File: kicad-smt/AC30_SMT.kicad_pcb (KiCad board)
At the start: 2 copper layers, 173 x 82 mm, 119 parts, among them IC1 4013, IC10 555, IC11 4001, IC12 1489, IC13 4070, IC14 4053, IC15 1488, IC2 4001, IC3 4070, IC4 4558, IC5 4013, IC6 4053, IC7 4049, IC8 4013, IC9 4023, J1 Front panel harness 1, J12 Power input, J2 Front panel harness 2, J3 Computer interface (COMP), J4 Control interface, J5 Terminal interface (TERM), Q1 MMBT5088, Q10 MMBT5087, Q11 MMBT5087, Q2 MMBT5088, Q3 MMBT5087, Q4 MMBT5088, Q5 MMBT5088, Q6 MMBT5088, Q7 MMBT5088, Q8 MMBT5088, Q9 MMBT5087

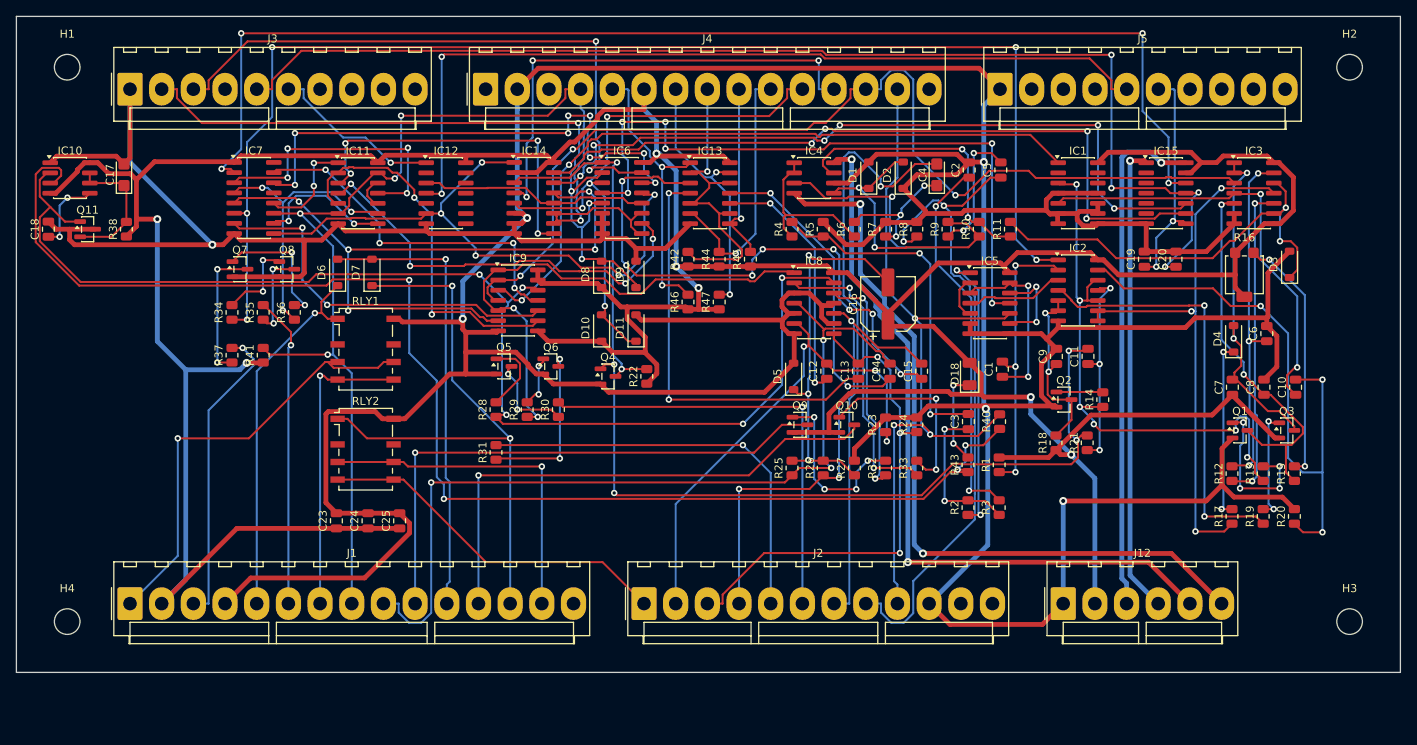
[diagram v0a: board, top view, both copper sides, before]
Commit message: SMT board: through-hole jumper pads for the front panel
Replace the J1/J2 KK-396 front-panel harness headers on the SMT board with
five rows of 0.1 in through-hole wire pads along the bottom edge, each pad
labelled with its net name on the silkscreen:
J1 SWITCHES, J2 LEDS, J13 MOTOR, J14 MIC (AUDIO_OUT), J15 EAR (AUDIO_IN).

The through-hole board keeps J1/J2. SMT board is now 173.0 x 89.0 mm;
ERC, DRC (all severities) and parity clean, fully routed.
AC30-SMT-settings.md updated.

Co-Authored-By: Claude Opus 5.5 <noreply@anthropic.com>
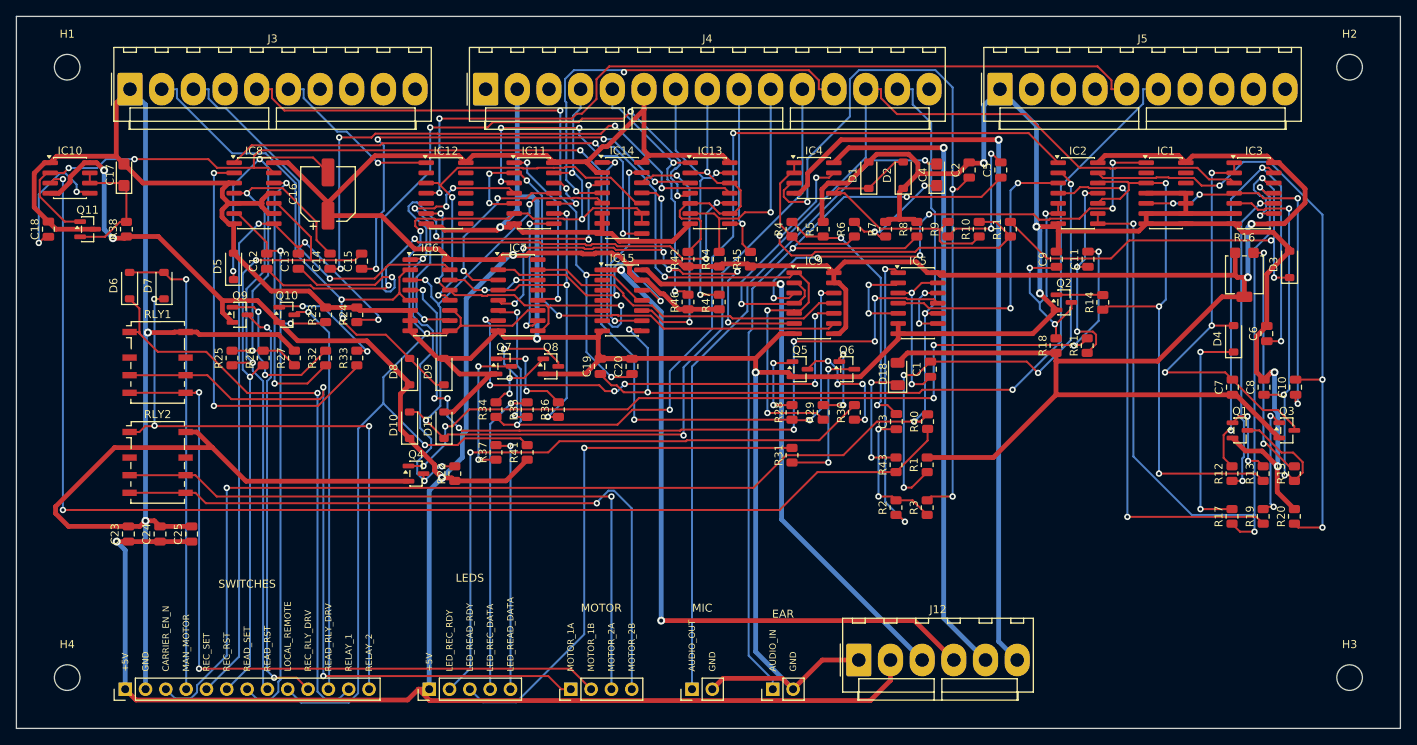
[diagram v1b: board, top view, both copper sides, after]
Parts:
- added J13: MOTOR, Connector_PinHeader_2.54mm:PinHeader_1x04_P2.54mm_Vertical, F.Cu at (99.3, 113.6)
- added J14: MIC, Connector_PinHeader_2.54mm:PinHeader_1x02_P2.54mm_Vertical, F.Cu at (114.5, 113.6)
- added J15: EAR, Connector_PinHeader_2.54mm:PinHeader_1x02_P2.54mm_Vertical, F.Cu at (124.5, 113.6)
- J1: value Front panel harness 1 -> SWITCHES; footprint Connector_Molex:Molex_KK-396_A-41791-0015_1x15_P3.96mm_Vertical -> Connector_PinHeader_2.54mm:PinHeader_1x13_P2.54mm_Vertical
- J2: value Front panel harness 2 -> LEDS; footprint Connector_Molex:Molex_KK-396_A-41791-0012_1x12_P3.96mm_Vertical -> Connector_PinHeader_2.54mm:PinHeader_1x05_P2.54mm_Vertical
- moved C12 71.3 mm to (61.3, 60.1)
- moved Q10 71.3 mm to (63.8, 66.8)
- moved R24 71.3 mm to (72.5, 66.8)
- moved R33 71.3 mm to (72.5, 72.2)
- moved C13 71.3 mm to (65.2, 60.1)
- moved C15 71.3 mm to (73.2, 60.1)
- moved D5 71.3 mm to (57.1, 60.8)
- moved Q9 71.3 mm to (58.0, 66.8)
- moved R23 71.3 mm to (68.7, 66.8)
- moved R25 71.3 mm to (57.0, 72.2)
- moved R26 71.3 mm to (60.9, 72.2)
- moved R27 71.3 mm to (64.8, 72.2)
- moved R32 71.3 mm to (68.7, 72.2)
- moved C14 71.3 mm to (69.2, 60.1)
- moved C16 71.3 mm to (69.0, 51.7)
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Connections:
- J1 pad 1: /MOTOR_1A -> +5V
- J1 pad 11: /MAN_MOTOR -> /READ_RLY_DRV
- J1 pad 12: /READ_RLY_DRV -> /RELAY_1
- J1 pad 2: +5V -> GND
- J1 pad 3: /LED_READ_DATA -> CARRIER_EN_N
- J1 pad 4: GND -> /MAN_MOTOR
- J1 pad 5: /RELAY_1 -> /REC_SET
- J1 pad 6: /LED_REC_DATA -> /REC_RST
- J1 pad 7: /MOTOR_1B -> /READ_SET
- J1 pad 8: /LOCAL_REMOTE -> /READ_RST
- J1 pad 9: /READ_RST -> /LOCAL_REMOTE
- J2 pad 1: /MOTOR_2B -> +5V
- J2 pad 2: /READ_SET -> /LED_REC_RDY
- J2 pad 3: /REC_SET -> /LED_READ_RDY
- J2 pad 4: /REC_RST -> /LED_REC_DATA
- J2 pad 5: /LED_READ_RDY -> /LED_READ_DATA
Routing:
- net /CPU_RX: track 154.6 -> 30.7 mm, vias 4 -> 2
- net +5V: track 542.4 -> 657.7 mm
- net /TERM_RS232_IN: track 28.3 -> 109.4 mm, vias 2 -> 3
- net CARRIER_EN_N: track 95.6 -> 170.5 mm
- net /TERM_ECHO: track 93.1 -> 24.7 mm, vias 4 -> 2
- net GND: track 778.5 -> 713.4 mm, vias 6 -> 10
- net /TERM_TX_SEL: track 93.6 -> 30.3 mm, vias 6 -> 2
- net /CPU_RS232_IN: track 149.9 -> 86.6 mm, vias 4 -> 3
- net /TERM_CLK_OUT: track 73.1 -> 133.1 mm
- net /MOTOR_1B: track 37.9 -> 93.3 mm, vias 1 -> 2
- net /DATA_SEL: track 66.7 -> 12.0 mm, vias 8 -> 2
- net /READ_EN: track 65.5 -> 114.8 mm, vias 2 -> 4
- net /MOTOR_2B: track 44.7 -> 87.5 mm, vias 0 -> 1
- net /MOTOR_2A: track 42.9 -> 85.4 mm
- net DATA_IN: track 162.2 -> 119.8 mm, vias 5 -> 4
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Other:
- board size 173 x 82 mm -> 173 x 89 mm
- board text added: "+5V"
- board text added: "AUDIO_IN"
- board text added: "AUDIO_OUT"
- board text added: "CARRIER_EN_N"
- board text added: "GND"
- board text added: "LED_READ_DATA"
- board text added: "LED_READ_RDY"
- board text added: "LED_REC_DATA"
- board text added: "LED_REC_RDY"
- board text added: "LOCAL_REMOTE"
- board text added: "MAN_MOTOR"
- board text added: "MOTOR_1A"
- board text added: "MOTOR_1B"
- board text added: "MOTOR_2A"
- board text added: "MOTOR_2B"
- board text added: "READ_RLY_DRV"
- board text added: "READ_RST"
- board text added: "READ_SET"
- board text added: "REC_RLY_DRV"
- board text added: "REC_RST"
- board text added: "REC_SET"
- board text added: "RELAY_1"
- board text added: "RELAY_2"

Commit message: SMT board: separate MIC A/B and EAR A/B jumper pads
Each front-panel jack now has its own tip and GND pads (J14 MIC: MIC_A,
GND, MIC_B, GND; J15 EAR: EAR_A, GND, EAR_B, GND). The S2/S3 audio poles
wire to new SWITCHES pads (AUDIO_OUT, MIC_A/B, AUDIO_IN, EAR_A/B) and the
board joins them. SMT board is now 173.0 x 88.5 mm; ERC, DRC (all
severities) and parity clean, fully routed. AC30-SMT-settings.md updated.

Co-Authored-By: Claude Opus 5.5 <noreply@anthropic.com>
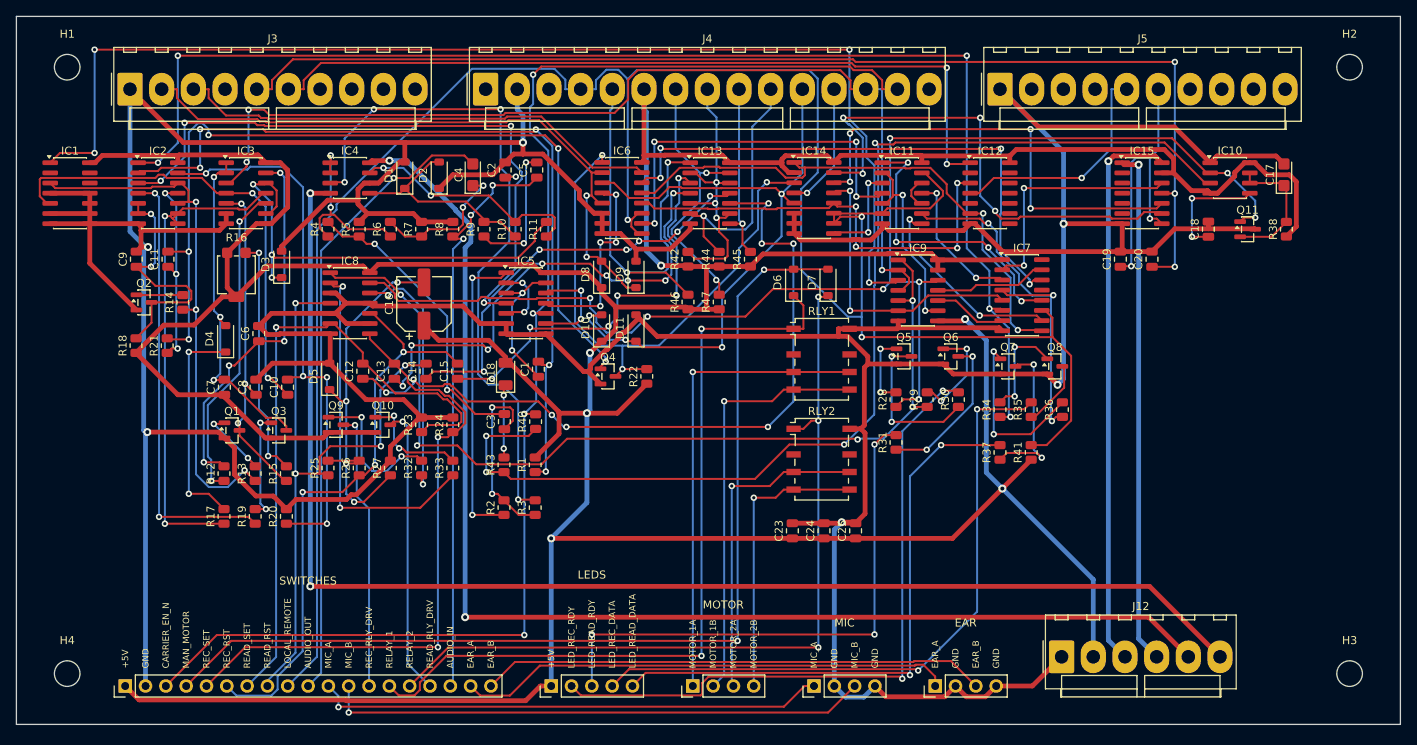
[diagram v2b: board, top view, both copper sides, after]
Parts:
- J1: footprint Connector_PinHeader_2.54mm:PinHeader_1x13_P2.54mm_Vertical -> Connector_PinHeader_2.54mm:PinHeader_1x19_P2.54mm_Vertical
- J14, J15: footprint Connector_PinHeader_2.54mm:PinHeader_1x02_P2.54mm_Vertical -> Connector_PinHeader_2.54mm:PinHeader_1x04_P2.54mm_Vertical
- moved C17 145.0 mm to (188.4, 49.3)
- moved C18 145.0 mm to (179.0, 56.1)
- moved IC10 145.0 mm to (181.7, 49.7)
- moved Q11 145.0 mm to (183.9, 56.1)
- moved R38 145.0 mm to (188.8, 56.1)
- moved IC1 137.0 mm to (36.7, 51.6)
- moved C6 126.0 mm to (60.3, 69.2)
- moved Q3 126.0 mm to (62.8, 81.2)
- moved C10 126.0 mm to (63.9, 75.8)
- moved C7 126.0 mm to (56.0, 75.8)
- moved D3 126.0 mm to (63.1, 60.5)
- moved D4 126.0 mm to (56.1, 69.8)
- moved R13 126.0 mm to (59.9, 86.7)
- moved R15 126.0 mm to (63.8, 86.7)
- moved R16 126.0 mm to (57.5, 61.8)
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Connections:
- J1 pad 10: /REC_RLY_DRV -> AUDIO_OUT
- J1 pad 11: /READ_RLY_DRV -> /MIC_A
- J1 pad 12: /RELAY_1 -> /MIC_B
- J1 pad 13: /RELAY_2 -> /REC_RLY_DRV
- J14 pad 1: AUDIO_OUT -> /MIC_A
- J15 pad 1: AUDIO_IN -> /EAR_A
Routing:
- net /LOCAL_REMOTE: track 163.9 -> 276.2 mm, vias 5 -> 3
- net DATA_OUT: track 63.9 -> 147.8 mm, vias 6 -> 4
- net /CPU_RS232_OUT: track 21.7 -> 99.6 mm, vias 1 -> 2
- net +7.5V: track 80.7 -> 157.9 mm, vias 1 -> 2
- net /TERM_RS232_IN: track 109.4 -> 35.3 mm, vias 3 -> 2
- net CLOCK_IN: track 98.6 -> 24.7 mm, vias 8 -> 4
- net -7.5V: track 95.2 -> 169.0 mm, vias 1 -> 2
- net /TERM_RS232_OUT: track 102.9 -> 29.3 mm, vias 2 -> 1
- net /MAN_MOTOR: track 58.7 -> 127.0 mm, vias 1 -> 2
- net /MIC_B: track 0.00 -> 67.9 mm, vias 0 -> 1
- net /MIC_A: track 0.00 -> 63.7 mm, vias 0 -> 1
- net /EAR_B: track 0.00 -> 63.2 mm
- net /EAR_A: track 0.00 -> 62.0 mm
- net /CPU_RS232_IN: track 86.6 -> 147.2 mm
- net /DATA_SEL: track 12.0 -> 69.2 mm, vias 2 -> 4
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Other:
- board size 173 x 89 mm -> 173 x 88.5 mm
- board text added: "EAR_A"
- board text added: "EAR_B"
- board text added: "MIC_A"
- board text added: "MIC_B"
